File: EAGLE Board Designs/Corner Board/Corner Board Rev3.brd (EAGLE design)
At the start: 100 x 50 mm, 40 parts, among them J1 CONNECTOR-8_AMPHENOL_M12A_08P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, J2 CONNECTOR-2_MICROFIT_SMD_RIGH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, J3 CONNECTOR-4_AMPHENOL_M12A_04P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, J4 CONNECTOR-4_μF_S_RA_, J5 CONNECTOR-4_μF_S_RA_, U1 VOLTAGE_REGULATOR_SOT-89_15V, U2 OPAMP_1_CHANNEL_OPA991, U3 INA823DT, U4 OPAMP_1_CHANNEL_OPA991, U5 OPAMP_1_CHANNEL_OPA991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

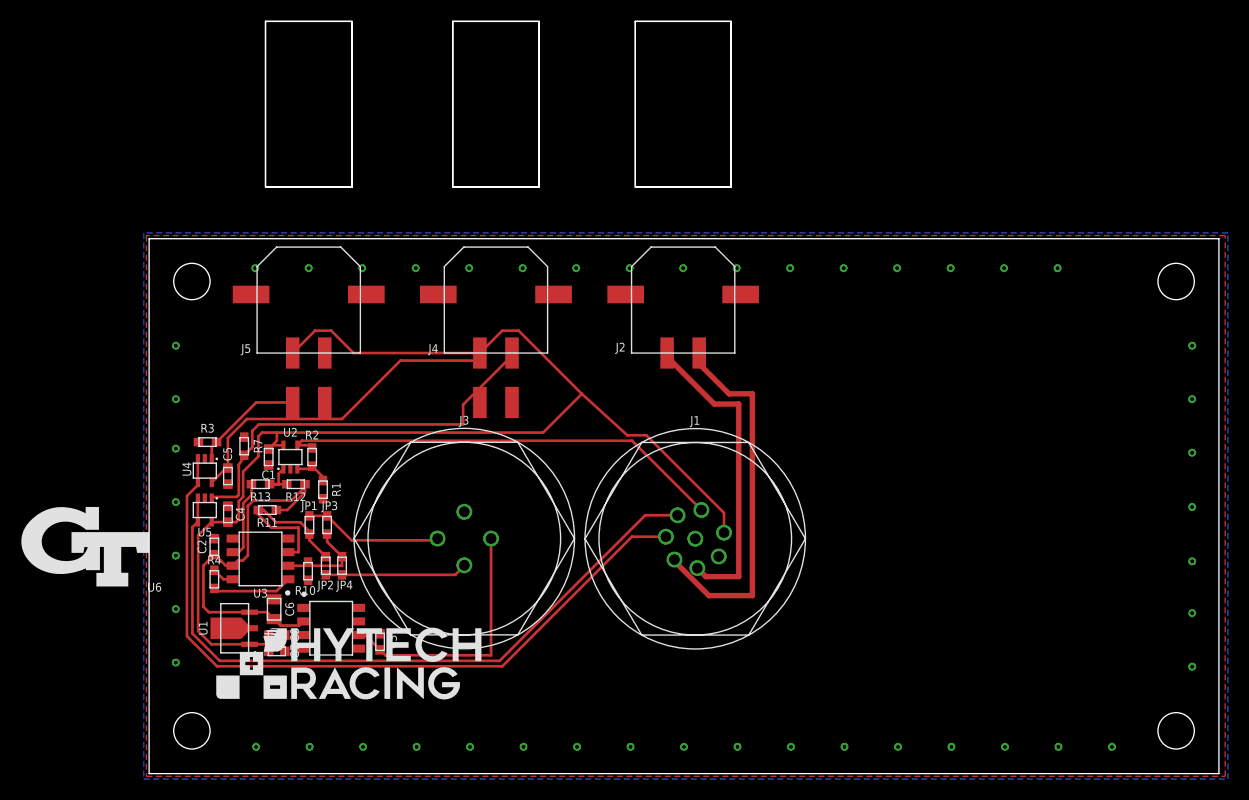
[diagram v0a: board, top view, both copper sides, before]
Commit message: Update CornerRev3
Added border and moved some components.
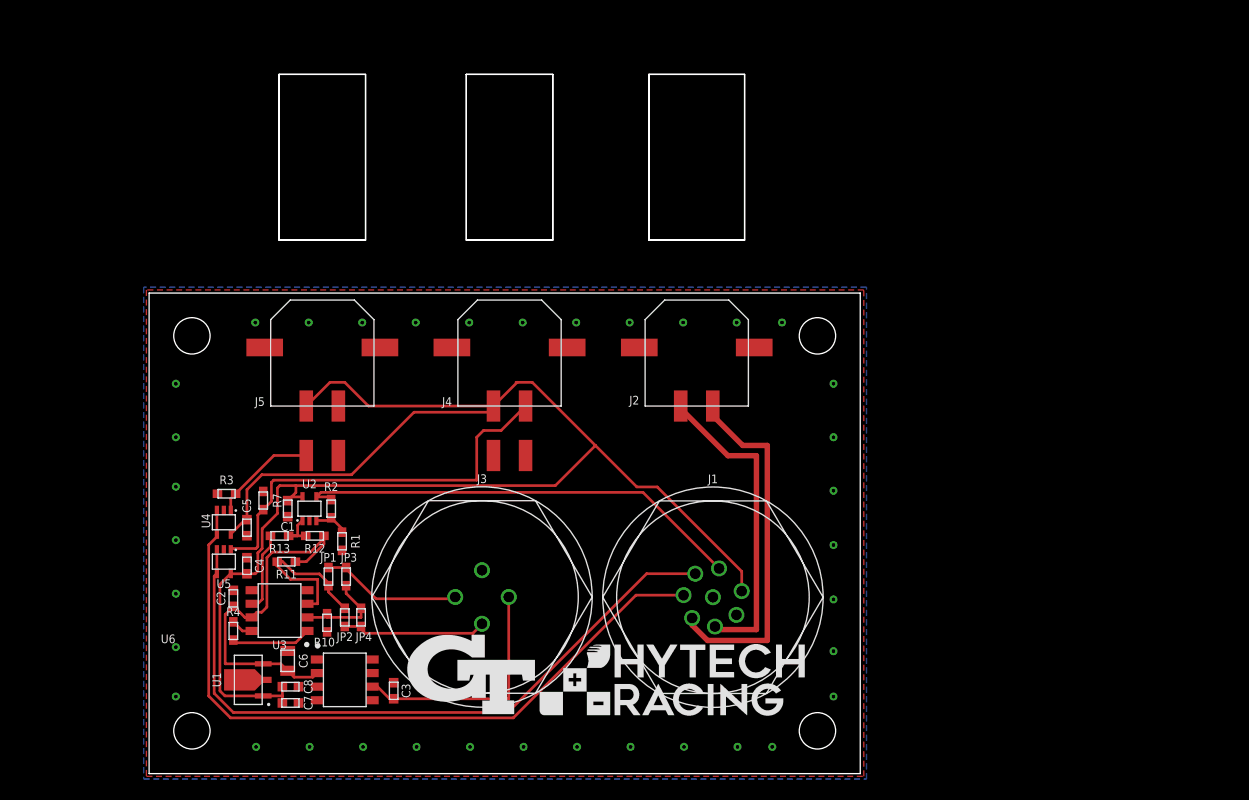
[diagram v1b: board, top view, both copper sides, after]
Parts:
- moved U$14 38.0 mm to (30.1, 9.27)
- moved U$8 33.9 mm to (62.5, 40.9)
- moved U$9 33.5 mm to (62.5, 4.00)
- moved U$13 30.3 mm to (36.4, 5.46)
- moved U$6 7.00 mm to (59.6, 25.7)
- moved J1 5.71 mm to (52.7, 16.5)
- moved J3 5.71 mm to (31.1, 16.5)
- moved R7 5.38 mm to (10.7, 25.5)
- moved C1 5.14 mm to (13.0, 24.8)
- moved C4 5.14 mm to (9.14, 19.4)
- moved C5 5.14 mm to (9.14, 23.0)
- moved JP4 5.14 mm to (19.8, 14.6)
- moved R11 5.14 mm to (12.8, 19.8)
- moved R2 5.14 mm to (17.0, 24.8)
- moved U2 5.14 mm to (15.0, 24.8)
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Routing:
- net 10V: track 24.0 -> 22.7 mm
- net PREINTERLOCK: track 34.8 -> 33.7 mm
- net SUS_POT_1: track 37.6 -> 38.2 mm
- net 15V: track 34.7 -> 34.1 mm
- net SUS_POT_2: track 10.4 -> 9.84 mm
- net +24V: track 148.3 -> 147.7 mm
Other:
- board size 100 x 50 mm -> 66.5 x 44.9 mm
- board text added: "Corner Board rev2 Designed by: Liwei Sun Shayan Noorani Mikhail Allen Brendan Bassett Ivan Mix"
- board text removed: "Corner Board rev2 Designed by: Liwei Sun Shayan Noorani Mikhail Allen Brendan Bassett"

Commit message: Finalized Corner Board Rev3
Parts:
- removed U$13: (no value), HyTechManufacturing:LOGO_HYTECH_MEDIUM
- added U$19: (no value), HyTechManufacturing:LOGO_HYTECH_SMALL
- U$14: device HyTechManufacturing:LOGO_GT_MEDIUM -> HyTechManufacturing:LOGO_GT_SMALL
- moved U$14 24.6 mm to (45.2, 28.7)
- moved R2 4.89 mm to (21.8, 24.0)
- moved C3 2.71 mm to (23.4, 5.08)
- moved R7 2.56 mm to (9.53, 23.2)
- moved R3 2.41 mm to (4.83, 26.2)
- moved U6 2.32 mm to (18.7, 6.48)
- moved R1 2.29 mm to (20.3, 21.6), turned to 0 degrees
- moved U5 2.22 mm to (4.83, 19.3)
- moved C7 2.16 mm to (13.3, 4.45)
- moved U4 2.16 mm to (4.83, 23.5)
- moved C4 2.09 mm to (7.11, 18.9), turned to 270 degrees
- moved U2 2.09 mm to (17.0, 24.3)
- moved JP2 1.92 mm to (18.0, 12.7)
- moved JP4 1.91 mm to (19.8, 12.7)
- moved C5 1.78 mm to (7.37, 23.1)
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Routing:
- net N$9: track 16.8 -> 9.68 mm
- net 10V: track 22.7 -> 18.9 mm
- net N$1: track 3.25 -> 5.99 mm
- net LOAD_CELL_AMPLIFIED: track 42.2 -> 39.6 mm
- net 15V: track 34.1 -> 36.8 mm
- net SUS_POT_2_24V: track 67.6 -> 70.2 mm
- net SUS_POT_1_24V: track 64.6 -> 66.3 mm
- net SUS_POT_1: track 38.2 -> 36.6 mm
- net N$7: track 9.04 -> 10.5 mm
- net SUS_POT_2: track 9.84 -> 11.2 mm
- net +24V: track 147.7 -> 146.4 mm
- net N$3: track 7.77 -> 8.53 mm
- net POSTINTERLOCK: track 29.4 -> 28.8 mm
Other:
- board size 66.5 x 44.9 mm -> 66 x 44.5 mm

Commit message: FINISHED Corner Board Rev3
Fixed minor mistakes.
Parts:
- moved R2 1.27 mm to (20.6, 24.0)
- moved C3 0.25 mm to (23.6, 5.08)
- moved R7 0.13 mm to (9.40, 23.2)
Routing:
- net N$1: track 5.99 -> 4.73 mm
- net +24V: track 146.4 -> 147.2 mm

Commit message: minor adjustments
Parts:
- moved R11 2.69 mm to (16.3, 17.5), turned to 90 degrees
- moved JP1 1.02 mm to (18.0, 17.5)
- moved JP3 0.76 mm to (19.8, 17.5)
- moved J2 0.37 mm to (50.8, 39.4)
- moved J5 0.19 mm to (15.2, 39.4)
- moved J1 0.13 mm to (52.6, 15.0)
- moved J4 0.10 mm to (33.0, 39.4)
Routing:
- net N$9: track 9.36 -> 7.96 mm
- net SIGNAL+: track 13.1 -> 12.1 mm
